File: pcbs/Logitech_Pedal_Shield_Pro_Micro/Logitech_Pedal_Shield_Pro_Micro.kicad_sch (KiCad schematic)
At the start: 11 parts, among them J1 DE9_Receptacle_MountingHoles, J2 AVR-ISP-6, U1 SparkFun_ProMicro

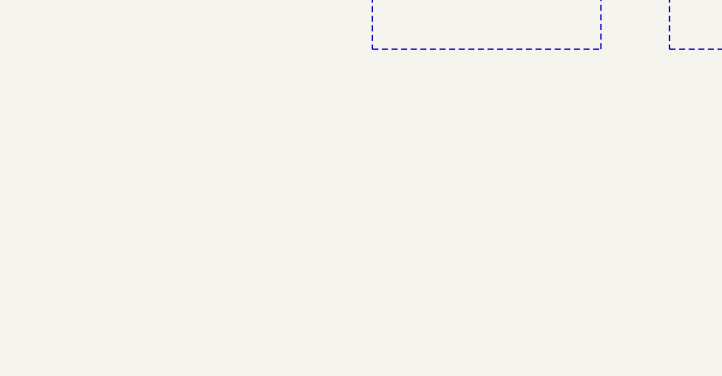
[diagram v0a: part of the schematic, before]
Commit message: Pedals: Update PCB version to v2.0.0
Matching the shifter, just so that the major repo version matches the PCB version to avoid confusion. No functional changes.
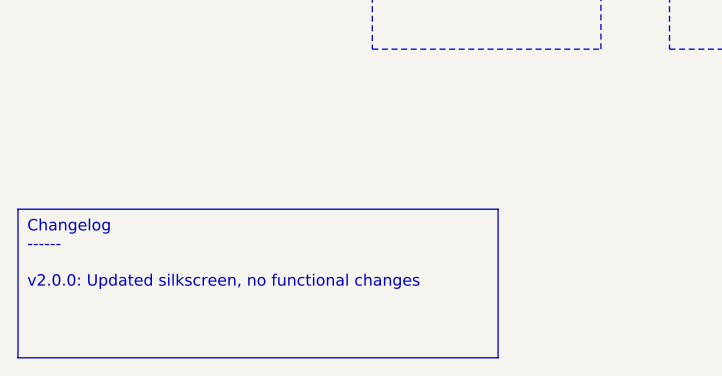
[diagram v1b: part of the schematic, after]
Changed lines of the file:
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@@
 	(title_block
 		(title "Logitech Pedal Shield for Pro Micro")
-		(date "2022-10-06")
-		(rev "v1.0.0")
+		(date "2025-03-31")
+		(rev "v2.0.0")
 	)
 	(junction
@@
 		)
 	)
+	(text_box "Changelog\n------\n\nv2.0.0: Updated silkscreen, no functional changes"
+		(exclude_from_sim no)
+		(at 15.24 177.8 0)
+		(size 53.34 16.51)
+		(stroke
+			(width 0)
+			(type default)
+		)
+		(fill
+			(type none)
+		)
+		(effects
+			(font
+				(size 1.27 1.27)
+			)
+			(justify left top)
+		)
+	)
